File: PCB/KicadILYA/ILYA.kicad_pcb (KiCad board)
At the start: 2 copper layers, 6 parts

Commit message: PCB NODEMCU + PCB WEMOS
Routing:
- net (no net): track 133.0 -> 135.3 mm
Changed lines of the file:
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@@
     (thickness 1.6)
     (drawings 13)
-    (tracks 35)
+    (tracks 33)
     (zones 0)
     (modules 6)
@@
     (pad_drill 0.6)
     (pad_to_mask_clearance 0)
+    (solder_mask_min_width 0.25)
     (aux_axis_origin 0 0)
     (visible_elements FFFFF77F)
@@
     (effects (font (size 1.5 1.5) (thickness 0.3)))
   )
-  (segment (start 116.84 97.79) (end 114.3 100.33) (width 0.25) (layer B.Cu) (net 0))
-  (segment (start 114.3 100.33) (end 106.68 100.33) (width 0.25) (layer B.Cu) (net 0))
-  (segment (start 120.65 92.71) (end 129.54 92.71) (width 0.25) (layer B.Cu) (net 0))
-  (segment (start 118.11 99.06) (end 118.11 95.25) (width 0.25) (layer B.Cu) (net 0))
-  (segment (start 118.11 95.25) (end 120.65 92.71) (width 0.25) (layer B.Cu) (net 0))
-  (segment (start 114.3 102.87) (end 118.11 99.06) (width 0.25) (layer B.Cu) (net 0))
-  (segment (start 116.84 107.95) (end 121.92 102.87) (width 0.25) (layer B.Cu) (net 0))
-  (segment (start 121.92 102.87) (end 121.92 97.79) (width 0.25) (layer B.Cu) (net 0))
-  (segment (start 124.46 95.25) (end 129.54 95.25) (width 0.25) (layer B.Cu) (net 0))
-  (segment (start 121.92 97.79) (end 124.46 95.25) (width 0.25) (layer B.Cu) (net 0))
-  (segment (start 116.84 114.3) (end 116.84 107.95) (width 0.25) (layer B.Cu) (net 0))
-  (segment (start 114.3 114.3) (end 114.3 102.87) (width 0.25) (layer B.Cu) (net 0))
-  (segment (start 110.32 82.55) (end 111.76 83.99) (width 0.25) (layer B.Cu) (net 0))
-  (segment (start 106.68 82.55) (end 110.32 82.55) (width 0.25) (layer B.Cu) (net 0))
-  (segment (start 129.54 82.55) (end 125.73 82.55) (width 0.25) (layer B.Cu) (net 0))
-  (segment (start 125.73 82.55) (end 124.46 83.82) (width 0.25) (layer B.Cu) (net 0))
-  (segment (start 129.54 85.09) (end 128.27 85.09) (width 0.25) (layer B.Cu) (net 0))
-  (segment (start 128.27 85.09) (end 125.73 87.63) (width 0.25) (layer B.Cu) (net 0))
-  (segment (start 123.19 114.3) (end 121.92 114.3) (width 0.25) (layer B.Cu) (net 0))
-  (segment (start 129.54 118.11) (end 127 118.11) (width 0.25) (layer B.Cu) (net 0))
-  (segment (start 127 118.11) (end 123.19 114.3) (width 0.25) (layer B.Cu) (net 0))
-  (segment (start 124.46 86.36) (end 124.46 83.82) (width 0.25) (layer B.Cu) (net 0))
-  (segment (start 125.73 87.63) (end 124.46 88.9) (width 0.25) (layer B.Cu) (net 0))
+  (segment (start 106.68 82.55) (end 110.32 82.55) (width 0.5) (layer B.Cu) (net 0))
   (segment (start 121.92 86.36) (end 121.92 87.63) (width 0.25) (layer B.Cu) (net 0))
-  (segment (start 121.92 87.63) (end 123.19 88.9) (width 0.25) (layer B.Cu) (net 0))
-  (segment (start 123.19 88.9) (end 124.46 88.9) (width 0.25) (layer B.Cu) (net 0))
-  (segment (start 111.76 83.99) (end 111.76 86.36) (width 0.25) (layer B.Cu) (net 0))
-  (segment (start 116.84 86.36) (end 116.84 97.79) (width 0.25) (layer B.Cu) (net 0))
-  (segment (start 114.3 86.36) (end 114.3 88.9) (width 0.25) (layer B.Cu) (net 0))
-  (segment (start 114.3 88.9) (end 113.03 90.17) (width 0.25) (layer B.Cu) (net 0))
-  (segment (start 113.03 90.17) (end 111.76 90.17) (width 0.25) (layer B.Cu) (net 0))
-  (segment (start 111.76 90.17) (end 109.22 87.63) (width 0.25) (layer B.Cu) (net 0))
-  (segment (start 109.22 87.63) (end 109.22 86.36) (width 0.25) (layer B.Cu) (net 0))
-  (segment (start 109.22 86.36) (end 107.95 85.09) (width 0.25) (layer B.Cu) (net 0))
-  (segment (start 107.95 85.09) (end 106.68 85.09) (width 0.25) (layer B.Cu) (net 0))
+  (segment (start 111.76 86.36) (end 111.76 83.82) (width 0.5) (layer B.Cu) (net 0))
+  (segment (start 111.76 83.82) (end 110.49 82.55) (width 0.5) (layer B.Cu) (net 0))
+  (segment (start 124.46 86.36) (end 124.46 83.82) (width 0.5) (layer B.Cu) (net 0))
+  (segment (start 125.73 82.55) (end 124.46 83.82) (width 0.5) (layer B.Cu) (net 0))
+  (segment (start 129.54 82.55) (end 125.73 82.55) (width 0.5) (layer B.Cu) (net 0))
+  (segment (start 129.54 85.09) (end 124.46 90.17) (width 0.5) (layer B.Cu) (net 0))
+  (segment (start 123.19 90.17) (end 124.46 90.17) (width 0.5) (layer B.Cu) (net 0))
+  (segment (start 121.92 88.9) (end 121.92 86.36) (width 0.5) (layer B.Cu) (net 0))
+  (segment (start 123.19 90.17) (end 121.92 88.9) (width 0.5) (layer B.Cu) (net 0))
+  (segment (start 129.54 118.11) (end 127 118.11) (width 0.5) (layer B.Cu) (net 0))
+  (segment (start 127 118.03) (end 127 118.11) (width 0.5) (layer B.Cu) (net 0))
+  (segment (start 123.27 114.3) (end 127 118.03) (width 0.5) (layer B.Cu) (net 0))
+  (segment (start 121.92 114.3) (end 123.27 114.3) (width 0.5) (layer B.Cu) (net 0))
+  (segment (start 114.3 86.36) (end 114.3 88.9) (width 0.5) (layer B.Cu) (net 0))
+  (segment (start 114.3 88.9) (end 113.03 90.17) (width 0.5) (layer B.Cu) (net 0))
+  (segment (start 111.76 90.17) (end 113.03 90.17) (width 0.5) (layer B.Cu) (net 0))
+  (segment (start 109.22 87.63) (end 111.76 90.17) (width 0.5) (layer B.Cu) (net 0))
+  (segment (start 109.22 87.63) (end 106.68 85.09) (width 0.5) (layer B.Cu) (net 0))
+  (segment (start 116.84 97.79) (end 114.3 100.33) (width 0.5) (layer B.Cu) (net 0))
+  (segment (start 116.84 86.36) (end 116.84 97.79) (width 0.5) (layer B.Cu) (net 0))
+  (segment (start 114.3 100.33) (end 106.68 100.33) (width 0.5) (layer B.Cu) (net 0))
+  (segment (start 120.65 92.71) (end 129.54 92.71) (width 0.5) (layer B.Cu) (net 0))
+  (segment (start 120.65 92.71) (end 118.11 95.25) (width 0.5) (layer B.Cu) (net 0))
+  (segment (start 118.11 99.06) (end 118.11 95.25) (width 0.5) (layer B.Cu) (net 0))
+  (segment (start 118.11 99.06) (end 114.3 102.87) (width 0.5) (layer B.Cu) (net 0))
+  (segment (start 114.3 102.87) (end 114.3 114.3) (width 0.5) (layer B.Cu) (net 0))
+  (segment (start 116.84 114.3) (end 116.84 107.95) (width 0.5) (layer B.Cu) (net 0))
+  (segment (start 116.84 107.95) (end 121.92 102.87) (width 0.5) (layer B.Cu) (net 0))
+  (segment (start 121.92 102.87) (end 121.92 97.79) (width 0.5) (layer B.Cu) (net 0))
+  (segment (start 121.92 97.79) (end 124.46 95.25) (width 0.5) (layer B.Cu) (net 0))
+  (segment (start 124.46 95.25) (end 129.54 95.25) (width 0.5) (layer B.Cu) (net 0))
 )

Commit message: Routage Bon mais connexion pins?
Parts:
- removed NODEMCU_Shield: VAL**, nodemcu:SEEED_113990105
- removed the REF** at (111.8, 86.4)
- removed the REF** at (129.5, 82.5)
- removed the REF** at (106.7, 82.5)
- removed the REF** at (121.9, 86.4)
- removed the REF** at (121.9, 114.3)
- added REF**: PinSocket_1x15_P2.54mm_Vertical, pinSocket:PinSocket_1x15_P2.54mm_Vertical, F.Cu at (81.3, 64.8)
- added REF**: PinSocket_1x15_P2.54mm_Vertical, pinSocket:PinSocket_1x15_P2.54mm_Vertical, F.Cu at (58.4, 64.8)
- added U1: NodeMCU1.0(ESP-12E), nodemcu:SEEED_113990105, F.Cu at (69.8, 82.5)
- added U101: Temperature_connector, pinHeads:PinHeader_1x04_P2.54mm_Horizontal, F.Cu at (77.5, 96.5)
- added U2: Relay_2_pins, pinHeads:PinHeader_1x02_P2.54mm_Horizontal, F.Cu at (66.0, 96.5)
- added U3101: Flow_connector, pinHeads:PinHeader_1x03_P2.54mm_Horizontal, F.Cu at (67.3, 68.6)
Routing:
- net (no net): track 135.3 -> 0.00 mm
- net VCC: track 0.00 -> 66.2 mm
- net GND: track 0.00 -> 46.7 mm
- net Net-(U1-Pad1): track 0.00 -> 35.0 mm
- net Net-(U1-Pad23): track 0.00 -> 17.5 mm
- net +5V: track 0.00 -> 8.57 mm
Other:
- rule trace_min: 0.2 -> 0.1
- rule via_min_size: 0.4 -> 0.1
- board text added: "NodeMCU Sheild"
- board text added: "P1"
- board text added: "P30"
- board text added: "Temp"
- board text removed: "1"
- board text removed: "GND"
- board text removed: "NC"
- board text removed: "SIG"
- board text removed: "Temperature"
- board text removed: "VCC"
- board text removed: "VIN"

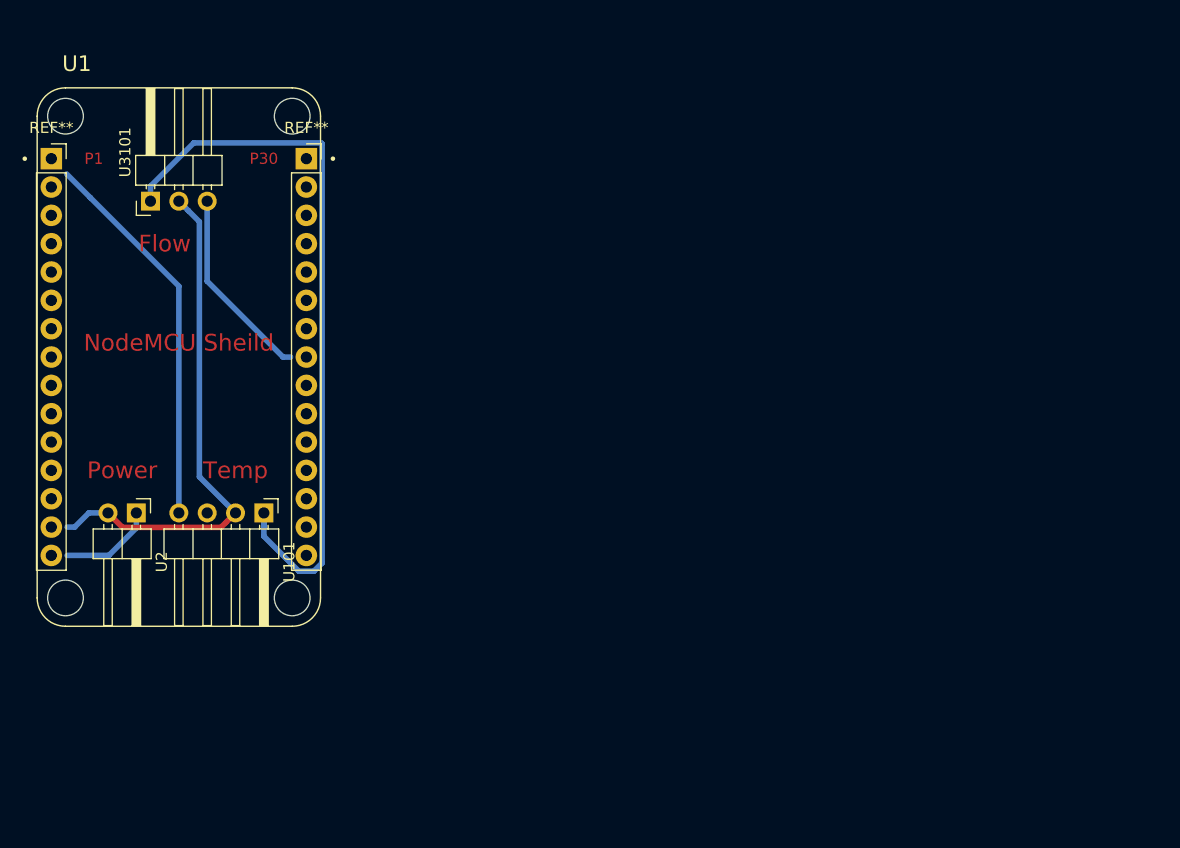
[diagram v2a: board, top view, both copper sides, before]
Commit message: Sheild esp8266 good
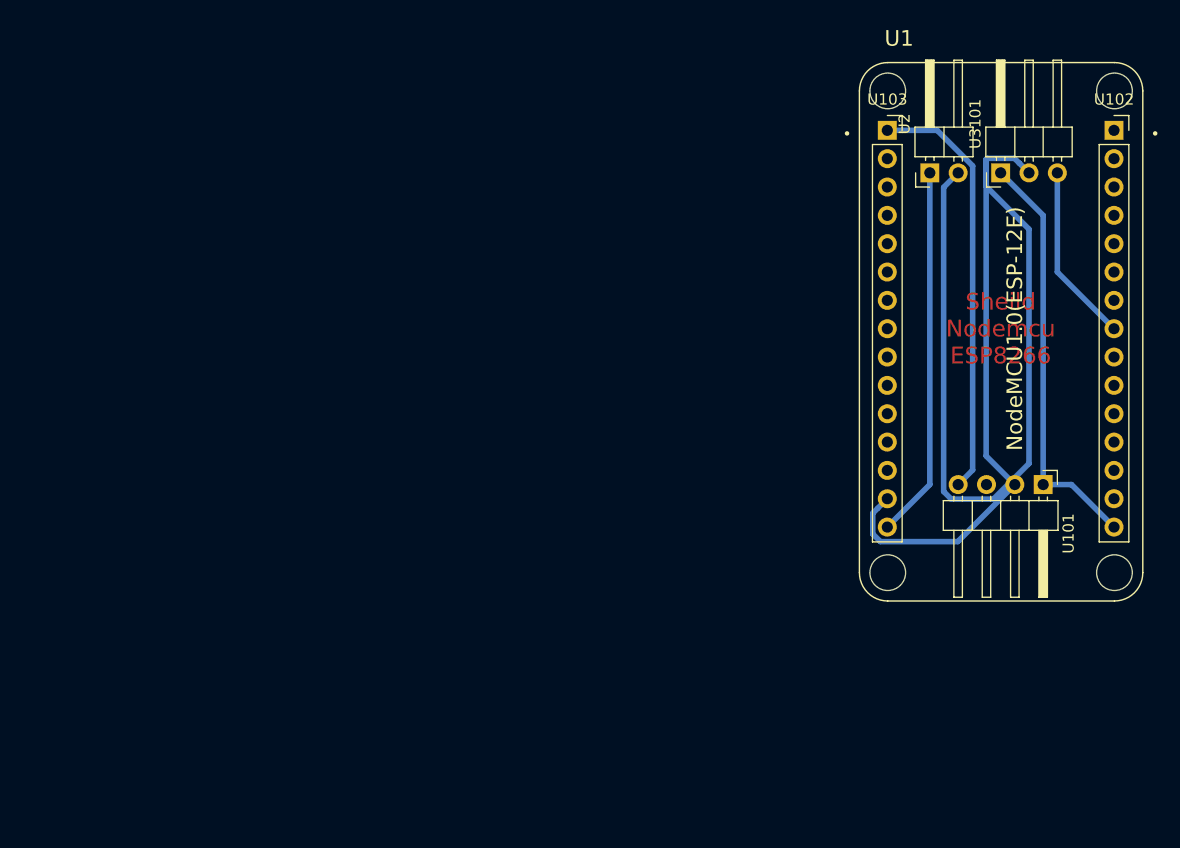
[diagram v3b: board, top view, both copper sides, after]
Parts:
- removed REF** (x2): PinSocket_1x15_P2.54mm_Vertical, pinSocket:PinSocket_1x15_P2.54mm_Vertical
- added U102: Pin-SocketESP8266_1x15_2, pinSocket:PinSocket_1x15_P2.54mm_Vertical2, F.Cu at (153.7, 62.2)
- added U103: Pin-SocketESP8266_1x15, pinSocket:PinSocket_1x15_P2.54mm_Vertical, F.Cu at (133.3, 62.2)
- U1: footprint nodemcu:SEEED_113990105 -> wemos-d1-mini:SEEED_113990105_withoutPin
- moved U2 77.4 mm to (137.2, 66.0), turned to 90 degrees
- moved U3101 76.2 mm to (143.5, 66.0)
- moved U1 73.7 mm to (143.6, 80.3)
- moved U101 69.9 mm to (147.3, 94.0)
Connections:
- U101 pad 4: Net-(U1-Pad1) -> SIGtemp
- U3101 pad 3: Net-(U1-Pad23) -> SIGFlow
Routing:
- net GND: track 46.7 -> 120.7 mm
- net SIGtemp: track 0.00 -> 38.1 mm
- net Net-(U1-Pad1): track 35.0 -> 0.00 mm
- net VCC: track 66.2 -> 37.4 mm
- net +5V: track 8.57 -> 33.3 mm
- net Net-(U1-Pad23): track 17.5 -> 0.00 mm
- net SIGFlow: track 0.00 -> 16.1 mm
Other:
- board text added: "Sheild Nodemcu ESP8266"
- board text removed: "Flow"
- board text removed: "NodeMCU Sheild"
- board text removed: "P1"
- board text removed: "P30"
- board text removed: "Power"
- board text removed: "Temp"
